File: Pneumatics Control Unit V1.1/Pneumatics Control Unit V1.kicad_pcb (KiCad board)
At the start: 2 copper layers, 35.8 x 27.4 mm, 38 parts, among them J1 TX_PORT, J2 10118194-0001LF, J3 RX_PORT, U1 SN65HVD1782D, U2 SN65HVD1782D, U3 FT2232D, Y1 Resonator_Small

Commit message: Linking foot prints
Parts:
- removed C10: 33n, Capacitor_SMD:C_0805_2012Metric_Pad1.18x1.45mm_HandSolder
- removed C9: 0.1u, Capacitor_SMD:C_0805_2012Metric_Pad1.18x1.45mm_HandSolder
- removed R10: 10k, Resistor_SMD:R_0805_2012Metric_Pad1.20x1.40mm_HandSolder
- removed R11: 1.5k, Resistor_SMD:R_0805_2012Metric_Pad1.20x1.40mm_HandSolder
- removed R8: 470, Resistor_SMD:R_0805_2012Metric_Pad1.20x1.40mm_HandSolder
- removed R9: 27, Resistor_SMD:R_0805_2012Metric_Pad1.20x1.40mm_HandSolder
- removed Y1: Resonator_Small, SamacSys_Parts:CSTCR_G
- added CR1: MBRS130L, MBRS130L:MBRS130L, F.Cu at (126.2, -194.4)
- added D10: D_TVS_x2_AAC, Package_TO_SOT_SMD:SOT-723, F.Cu at (141.1, -208.4)
- added D5: D_TVS_x2_AAC, Package_TO_SOT_SMD:SOT-723, F.Cu at (179.8, -213.7)
- added D6: D_TVS_x2_AAC, Package_TO_SOT_SMD:SOT-723, F.Cu at (167.0, -199.6)
- added D7: D_TVS_x2_AAC, Package_TO_SOT_SMD:SOT-723, F.Cu at (203.9, -235.5)
- added D8: D_TVS_x2_AAC, Package_TO_SOT_SMD:SOT-723, F.Cu at (186.7, -220.2)
- added D9: D_TVS_x2_AAC, Package_TO_SOT_SMD:SOT-723, F.Cu at (156.1, -188.8)
- added J10: Conn_01x02_Male, Connector_PinSocket_2.54mm:PinSocket_1x02_P2.54mm_Vertical, F.Cu at (182.9, -225.9)
- added J11: Conn_01x02_Male, Connector_PinSocket_2.54mm:PinSocket_1x02_P2.54mm_Vertical, F.Cu at (136.5, -191.4)
- added J4: Conn_01x02_Male, Connector_PinSocket_2.54mm:PinSocket_1x02_P2.54mm_Vertical, F.Cu at (141.1, -191.4)
- added J5: Conn_01x02_Male, Connector_PinSocket_2.54mm:PinSocket_1x02_P2.54mm_Vertical, F.Cu at (156.8, -201.6)
- added J6: Conn_01x02_Male, Connector_PinSocket_2.54mm:PinSocket_1x02_P2.54mm_Vertical, F.Cu at (152.2, -203.1)
- added J7: Conn_01x02_Male, Connector_PinSocket_2.54mm:PinSocket_1x02_P2.54mm_Vertical, F.Cu at (145.7, -191.4)
- added J8: Conn_01x02_Male, Connector_PinSocket_2.54mm:PinSocket_1x02_P2.54mm_Vertical, F.Cu at (136.5, -199.7)
- added J9: Conn_01x02_Male, Connector_PinSocket_2.54mm:PinSocket_1x02_P2.54mm_Vertical, F.Cu at (152.2, -196.0)
- added L1: SRR1205-500YL, induct:SRR1205500YL, F.Cu at (131.1, -209.9)
- added MOSFET1: SSM3K7002KFU, SSM3K7002KFU:SSM3K7002KFU, F.Cu at (176.3, -232.8)
- added MOSFET2: SSM3K7002KFU, SSM3K7002KFU:SSM3K7002KFU, F.Cu at (164.6, -220.2)
- added MOSFET3: SSM3K7002KFU, SSM3K7002KFU:SSM3K7002KFU, F.Cu at (144.1, -198.3)
- added MOSFET4: SSM3K7002KFU, SSM3K7002KFU:SSM3K7002KFU, F.Cu at (196.7, -232.8)
- added MOSFET5: SSM3K7002KFU, SSM3K7002KFU:SSM3K7002KFU, F.Cu at (174.8, -220.2)
- added MOSFET6: SSM3K7002KFU, SSM3K7002KFU:SSM3K7002KFU, F.Cu at (162.4, -208.5)
- added MOSFET7: SSM3K7002KFU, SSM3K7002KFU:SSM3K7002KFU, F.Cu at (172.6, -208.5)
- added MOSFET8: SSM3K7002KFU, SSM3K7002KFU:SSM3K7002KFU, F.Cu at (186.5, -232.8)
- C5: value 10n -> 100u; moved to F.Cu
- C6: value 10n -> 6.8n; moved to F.Cu
- C7: value 0.1u -> 0.01u; moved to F.Cu
- C8: value 0.1u -> 100u; moved to F.Cu
- D1: value RX_LED -> CDSOT23-SM712; footprint LED_SMD:LED_0805_2012Metric_Pad1.15x1.40mm_HandSolder -> CDSOT23-SM712:SOT-23-3
- D2: value TX_LED -> CDSOT23-SM712; footprint LED_SMD:LED_0805_2012Metric_Pad1.15x1.40mm_HandSolder -> CDSOT23-SM712:SOT-23-3
- D3, D4: value CDSOT23-SM712 -> D_TVS_x2_AAC; footprint CDSOT23-SM712:SOT-23-3 -> Package_TO_SOT_SMD:SOT-723
- J1: value TX_PORT -> RX_PORT; footprint Andrew_Custom:C189737 -> RS485:RS485
- J2: value 10118194-0001LF -> RX_PORT; footprint 10118194-0001LF:AMPHENOL_10118194-0001LF -> RS485:RS485
- J3: value RX_PORT -> MICROMOD-2222; footprint Andrew_Custom:C189737 -> m2:MDT420M02001
- R5, R6: value 330 -> 10000; moved to F.Cu
- R7: value 27 -> 10000; moved to F.Cu
- U1: value SN65HVD1782D -> ISL83490IBZ; footprint SN65HVD1782D:SOIC127P599X175-8N -> RS_UART:ISL83490IBZ
- U2: value SN65HVD1782D -> MIC2178-3.3YWM; footprint SN65HVD1782D:SOIC127P599X175-8N -> 33sw:MIC2178-3.3YWM
- U3: value FT2232D -> MC78M05CDTRKG; footprint Package_QFP:LQFP-48_7x7mm_P0.5mm -> 5v:MC78M05CDTRKG; moved to F.Cu
- moved R6 347.7 mm to (204.8, -238.4), turned to 0 degrees
- moved H2 344.1 mm to (188.4, -224.9)
- moved R7 338.6 mm to (194.1, -226.7), turned to 0 degrees
- moved U3 334.6 mm to (150.8, -230.8), turned to 0 degrees
- moved D4 334.4 mm to (182.6, -213.7), turned to 0 degrees
- moved J3 333.6 mm to (120.2, -227.2), turned to 0 degrees
- moved U1 331.8 mm to (166.3, -232.7), turned to 0 degrees
- moved R2 324.6 mm to (182.9, -216.6)
- moved R5 320.8 mm to (182.9, -219.6), turned to 0 degrees
- moved R3 316.0 mm to (168.0, -202.5)
- moved U2 310.9 mm to (115.3, -206.6), turned to 0 degrees
- moved J2 310.5 mm to (150.9, -210.3), turned to 0 degrees
- moved H3 307.0 mm to (157.7, -193.5)
- moved D2 305.5 mm to (141.5, -215.8), turned to 0 degrees
- moved C3 304.3 mm to (125.0, -200.5), turned to 0 degrees
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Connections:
- C1 pad 1: Net-(D3-Pad1) -> Net-(C1-Pad1)
- C2 pad 1: Net-(D3-Pad2) -> Net-(C2-Pad1)
- C3 pad 1: Net-(D4-Pad1) -> Net-(C3-Pad1)
- C4 pad 1: Net-(D4-Pad2) -> Net-(C4-Pad1)
- C5 pad 1: +5V -> GND
- C5 pad 2: GND -> /RS485_B_12V
- C6 pad 1: +5V -> Net-(C6-Pad1)
- C7 pad 1: +5V -> Net-(C7-Pad1)
- C8 pad 1: GND -> Net-(C8-Pad1)
- C8 pad 2: Net-(C9-Pad2) -> GND
- D1 pad 1: Net-(D1-Pad1) -> Net-(C1-Pad1)
- D1 pad 2: +5V -> Net-(C3-Pad1)
- D2 pad 1: Net-(D2-Pad1) -> Net-(C2-Pad1)
- D2 pad 2: +5V -> Net-(C4-Pad1)
- D3 pad 1: Net-(D3-Pad1) -> /GPIO_1
- D4 pad 1: Net-(D4-Pad1) -> /GPIO_0
- J1 pad 1: Net-(D3-Pad2) -> Net-(C3-Pad1)
- J1 pad 2: Net-(D3-Pad1) -> Net-(C1-Pad1)
- J1 pad 4: unconnected-(J1-Pad4) -> /RS485_B_12V
- J2 pad 1: +5V -> Net-(C4-Pad1)
- J2 pad 2: USB_D- -> Net-(C2-Pad1)
- J2 pad 3: USB_D+ -> GND
- J2 pad 4: GND -> /RS485_A_12V
- J3 pad 1: Net-(D4-Pad2) -> GND
- J3 pad 2: Net-(D4-Pad1) -> Net-(J3-Pad11)
- J3 pad 3: GND -> unconnected-(J3-Pad3)
- J3 pad 4: unconnected-(J2-Pad4) -> Net-(J3-Pad11)
- R1 pad 1: Net-(D3-Pad1) -> Net-(C3-Pad1)
- R1 pad 2: Net-(U2-Pad7) -> Net-(R1-Pad2)
- R2 pad 1: Net-(D3-Pad2) -> Net-(C1-Pad1)
- R2 pad 2: Net-(U2-Pad6) -> Net-(R2-Pad2)
- R3 pad 1: Net-(D4-Pad1) -> Net-(C4-Pad1)
- R3 pad 2: Net-(R4-Pad2) -> Net-(R3-Pad2)
- R4 pad 1: Net-(D4-Pad2) -> Net-(C2-Pad1)
- R4 pad 2: Net-(R3-Pad2) -> Net-(R4-Pad2)
- R5 pad 1: Net-(D2-Pad1) -> Net-(R5-Pad1)
- R5 pad 2: ~{USB_A_TXDLED} -> /RS485_B_12V
- R6 pad 1: Net-(D1-Pad1) -> Net-(R6-Pad1)
- R6 pad 2: ~{USB_A_RXDLED} -> Net-(C6-Pad1)
- R7 pad 1: USB_D- -> Net-(C7-Pad1)
- R7 pad 2: Net-(R7-Pad2) -> GND
- U1 pad 1: unconnected-(U2-Pad1) -> Net-(U1-Pad1)
- U1 pad 2: +5V -> /RS485_TXD
- U1 pad 3: +5V -> /RS485_RXD
- U1 pad 4: RS485_RXD -> Net-(U1-Pad4)
- U1 pad 5: GND -> Net-(R2-Pad2)
- U1 pad 6: Net-(U2-Pad6) -> Net-(R1-Pad2)
- U1 pad 7: Net-(U2-Pad7) -> Net-(R4-Pad2)
- U1 pad 8: +5V -> Net-(R3-Pad2)
- U2 pad 1: RS485_TXD -> /RS485_B_12V
- U2 pad 2: GND -> /RS485_B_12V
- U2 pad 3: GND -> Net-(U2-Pad3)
- U2 pad 4: unconnected-(U1-Pad4) -> GND
- U2 pad 6: Net-(R3-Pad2) -> GND
- U2 pad 7: Net-(R4-Pad2) -> GND
- U2 pad 8: +5V -> Net-(U2-Pad3)
- U3 pad 1: unconnected-(U3-Pad1) -> /RS485_A_12V
- U3 pad 3: +5V -> Net-(U3-Pad3)
- U3 pad 4: +5V -> GND
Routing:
- net GND: track 131.5 -> 0.00 mm, vias 15 -> 0
- net +5V: track 102.6 -> 0.00 mm, vias 3 -> 0
- net ~{USB_A_TXDLED}: track 46.5 -> 0.00 mm
- net ~{USB_A_RXDLED}: track 37.6 -> 0.00 mm
- net RS485_RXD: track 35.1 -> 0.00 mm, vias 1 -> 0
- net Net-(R7-Pad2): track 30.8 -> 0.00 mm
- net Net-(R8-Pad2): track 24.7 -> 0.00 mm
- net RS485_TXD: track 24.4 -> 0.00 mm, vias 1 -> 0
- net Net-(D4-Pad2): track 12.0 -> 0.00 mm
- net Net-(D3-Pad2): track 11.9 -> 0.00 mm
- net Net-(D4-Pad1): track 9.21 -> 0.00 mm
- net Net-(D3-Pad1): track 8.92 -> 0.00 mm
- net Net-(C9-Pad2): track 8.03 -> 0.00 mm
- net USB_D+: track 6.99 -> 0.00 mm, vias 1 -> 0
- net Net-(R10-Pad2): track 6.93 -> 0.00 mm
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- removed copper zone on B.Cu, net GND
- removed copper zone on F.Cu, net GND
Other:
- board outline removed

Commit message: Adding better m.2 connector
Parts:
- added C10: 0.1u, Capacitor_SMD:C_0805_2012Metric_Pad1.18x1.45mm_HandSolder, F.Cu at (127.2, 112.9)
- added C11: CL21A226MQQNNNF (22uF), 22U:CL21A226MQQNNNF, F.Cu at (195.9, 65.9)
- added C12: 22uF, 22U:CL21A226MQQNNNF, F.Cu at (171.2, 89.2)
- added C13: 22uF, 22U:CL21A226MQQNNNF, F.Cu at (171.2, 81.0)
- added C14: 22uF, 22U:CL21A226MQQNNNF, F.Cu at (178.5, 77.6)
- added C15: 22uF, 22U:CL21A226MQQNNNF, F.Cu at (195.6, 57.7)
- added C16: 22uF, 22U:CL21A226MQQNNNF, F.Cu at (150.4, 104.3)
- added C17: 22uF, 22U:CL21A226MQQNNNF, F.Cu at (188.6, 65.9)
- added C18: 22uF, 22U:CL21A226MQQNNNF, F.Cu at (157.7, 104.3)
- added C19: 22uF, 22U:CL21A226MQQNNNF, F.Cu at (150.4, 96.1)
- added C20: 22uF, 22U:CL21A226MQQNNNF, F.Cu at (157.7, 96.1)
- added C21: 22uF, 22U:CL21A226MQQNNNF, F.Cu at (188.3, 57.7)
- added C22: 1u, Capacitor_SMD:C_0805_2012Metric_Pad1.18x1.45mm_HandSolder, F.Cu at (129.6, 85.3)
- added C23: 1u, Capacitor_SMD:C_0805_2012Metric_Pad1.18x1.45mm_HandSolder, F.Cu at (150.0, 109.9)
- added C9: 0.1u, Capacitor_SMD:C_0805_2012Metric_Pad1.18x1.45mm_HandSolder, F.Cu at (141.6, 112.9)
- added H4: MountingHole, MountingHole:MountingHole_2.5mm, F.Cu at (190.8, 80.4)
- added H5: STAND-OFF-REFLOW2.5MM_TALL, MicroMod_ATP_CarrierBoard:STAND-OFF-REFLOW-M2.5, F.Cu at (110.4, 47.6)
- added J12: 10118194-0001LF, 10118194-0001LF:AMPHENOL_10118194-0001LF, F.Cu at (180.5, 70.1)
- C5, C8: value 100u -> 10n
- D1, D2: value CDSOT23-SM712 -> D_TVS_x2_AAC; footprint CDSOT23-SM712:SOT-23-3 -> Package_TO_SOT_SMD:SOT-723
- J3: footprint m2:MDT420M02001 -> mm-m:M.2-CONNECTOR-E
- L1: value SRR1205-500YL -> LB3218T330M (33uH); footprint induct:SRR1205500YL -> induct33u:LB3218T330M
- R5: value 10000 -> 20k
- R6, R7: value 10000 -> 10k
- U3: footprint 5v:MC78M05CDTRKG -> 12v5v:MC78M05CDTRKG
- moved MOSFET8 344.0 mm to (131.7, 106.8)
- moved MOSFET1 341.4 mm to (141.9, 106.8)
- moved R6 329.2 mm to (178.0, 89.7)
- moved R7 329.0 mm to (169.2, 101.4)
- moved D4 323.1 mm to (163.6, 108.8)
- moved H2 322.1 mm to (170.1, 96.6)
- moved D10 321.8 mm to (159.9, 112.8)
- moved MOSFET5 318.3 mm to (131.7, 95.2)
- moved C3 314.9 mm to (156.0, 112.9)
- moved C2 313.9 mm to (146.4, 112.9)
- moved U1 307.7 mm to (157.3, 75.0)
- moved D7 306.9 mm to (201.2, 71.4)
- moved R5 305.3 mm to (184.6, 85.7)
- moved MOSFET6 304.4 mm to (141.9, 95.2)
- moved CR1 301.7 mm to (116.8, 107.2)
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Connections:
- C5 pad 1: GND -> Net-(C10-Pad1)
- C5 pad 2: /RS485_B_12V -> GND
- C8 pad 1: Net-(C8-Pad1) -> Net-(C10-Pad1)
- CR1 pad 1: Net-(U2-Pad3) -> Net-(CR1-Pad1)
- J3 pad 3: unconnected-(J3-Pad3) -> /USB_D+
- J3 pad 5: unconnected-(J3-Pad5) -> /USB_D-
- J3 pad 9: unconnected-(J3-Pad9) -> Net-(J3-Pad9)
- L1 pad 1: Net-(U2-Pad3) -> /220uF
- L1 pad 2: Net-(C8-Pad1) -> Net-(CR1-Pad1)
- R5 pad 2: /RS485_B_12V -> /RS485_A_12V
- U2 pad 1: /RS485_B_12V -> /RS485_A_12V
- U2 pad 12: Net-(C8-Pad1) -> /220uF
- U2 pad 2: /RS485_B_12V -> /RS485_A_12V
- U2 pad 20: /RS485_B_12V -> /RS485_A_12V
- U2 pad 3: Net-(U2-Pad3) -> Net-(CR1-Pad1)
- U2 pad 8: Net-(U2-Pad3) -> Net-(CR1-Pad1)
- U2 pad 9: /RS485_B_12V -> /RS485_A_12V
- U3 pad 1: /RS485_A_12V -> /RS485_B_12V

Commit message: PCB Fun times :)
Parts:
- C1, C2, C3, C4, D1, D2, H5, J3, R1, R2, R3, R4, U1: moved to B.Cu
- moved R5 142.0 mm to (44.1, 106.0)
- moved C15 137.4 mm to (62.0, 89.7)
- moved C11 137.0 mm to (61.5, 92.5)
- moved C21 134.8 mm to (57.4, 89.9)
- moved C17 133.8 mm to (57.5, 92.5)
- moved C12 127.1 mm to (44.1, 92.2)
- moved C14 110.6 mm to (68.5, 89.3)
- moved C18 109.7 mm to (48.6, 92.5)
- moved C20 109.3 mm to (48.6, 89.5)
- moved R2 108.5 mm to (128.3, 118.5), turned to 180 degrees
- moved C13 104.1 mm to (67.8, 92.5)
- moved R1 99.1 mm to (129.7, 121.2), turned to 180 degrees
- moved C16 98.5 mm to (52.7, 92.3)
- moved C19 97.5 mm to (53.1, 89.9)
- moved J5 96.2 mm to (112.8, 75.5)
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
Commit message: Consolidated PCB
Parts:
- C10, C5, C8, C9, D10, D3, D4, D5, D6, D7, D8, D9, MOSFET1, MOSFET2, MOSFET3, MOSFET4, MOSFET5, MOSFET6, MOSFET7, MOSFET8: moved to B.Cu
- moved R5 77.9 mm to (119.9, 88.4), turned to 90 degrees
- moved C12 77.8 mm to (121.5, 100.1), turned to 90 degrees
- moved C16 74.3 mm to (126.6, 100.2), turned to 90 degrees
- moved C18 72.9 mm to (121.5, 95.5), turned to 90 degrees
- moved U2 71.2 mm to (130.2, 86.9)
- moved C20 70.0 mm to (118.4, 95.5), turned to 90 degrees
- moved C15 67.4 mm to (129.1, 95.7), turned to 90 degrees
- moved C21 67.4 mm to (124.0, 100.2), turned to 90 degrees
- moved C17 66.6 mm to (124.0, 95.7), turned to 90 degrees
- moved C19 66.1 mm to (118.4, 100.1), turned to 90 degrees
- moved CR1 65.1 mm to (130.7, 77.9)
- moved C6 62.7 mm to (137.7, 99.6), turned to 90 degrees
- moved C14 61.6 mm to (129.1, 100.1), turned to 90 degrees
- moved L1 59.7 mm to (122.9, 79.2)
- moved C13 58.9 mm to (126.6, 95.5), turned to 90 degrees
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
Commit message: Technically its wired
This is a little messy, but it is wired
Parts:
- moved MOSFET8 1.66 mm to (150.9, 91.0)
- moved D10 1.50 mm to (150.6, 88.0)
- moved MOSFET3 1.30 mm to (110.0, 102.6)
- moved D7 1.28 mm to (110.2, 109.0)
- moved U1 1.14 mm to (121.9, 114.8), turned to 0 degrees
- moved D5 1.14 mm to (110.0, 99.8)
- moved J11 1.09 mm to (154.2, 88.2)
- moved J7 1.08 mm to (154.3, 98.7)
- moved D6 1.08 mm to (150.9, 98.0)
- moved MOSFET4 1.08 mm to (151.2, 100.9)
- moved MOSFET5 1.02 mm to (110.2, 111.8)
- moved D9 0.95 mm to (150.5, 109.4)
- moved J10 0.95 mm to (153.9, 110.5)
- moved MOSFET7 0.95 mm to (150.6, 112.9)
- moved MOSFET1 0.88 mm to (110.0, 89.9)
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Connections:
- C23 pad 1: Net-(C23-Pad1) -> 5V
- J10 pad 2: Net-(J10-Pad2) -> 5V
- J11 pad 2: Net-(J11-Pad2) -> 5V
- J12 pad 1: Net-(J12-Pad1) -> USB_V
- J3 pad 9: Net-(J3-Pad9) -> USB_V
- J4 pad 2: Net-(J4-Pad2) -> 5V
- J5 pad 2: Net-(J5-Pad2) -> 5V
- J6 pad 2: Net-(J6-Pad2) -> 5V
- J7 pad 2: Net-(J7-Pad2) -> 5V
- J8 pad 2: Net-(J8-Pad2) -> 5V
- J9 pad 2: Net-(J9-Pad2) -> 5V
- U1 pad 1: Net-(U1-Pad1) -> 5V
- U3 pad 3: Net-(C23-Pad1) -> 5V
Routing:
- net GND: track 0.00 -> 393.8 mm, vias 0 -> 23
- net 5V: track 0.00 -> 195.8 mm, vias 0 -> 3
- net /RS485_A_12V: track 0.00 -> 84.7 mm, vias 0 -> 2
- net /USB_D-: track 0.00 -> 50.2 mm, vias 0 -> 5
- net /220uF: track 0.00 -> 47.6 mm, vias 0 -> 4
- net USB_V: track 0.00 -> 45.4 mm, vias 0 -> 3
- net /GPIO_4: track 0.00 -> 42.7 mm
- net /USB_D+: track 0.00 -> 42.2 mm, vias 0 -> 3
- net Net-(R6-Pad1): track 0.00 -> 41.8 mm, vias 0 -> 6
- net Net-(J3-Pad11): track 0.00 -> 41.4 mm, vias 0 -> 3
- net /GPIO_3: track 0.00 -> 38.0 mm
- net /GPIO_7: track 0.00 -> 36.0 mm, vias 0 -> 2
- net /GPIO_1: track 0.00 -> 32.7 mm, vias 0 -> 2
- net /GPIO_6: track 0.00 -> 32.3 mm, vias 0 -> 2
- net /GPIO_2: track 0.00 -> 31.7 mm
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
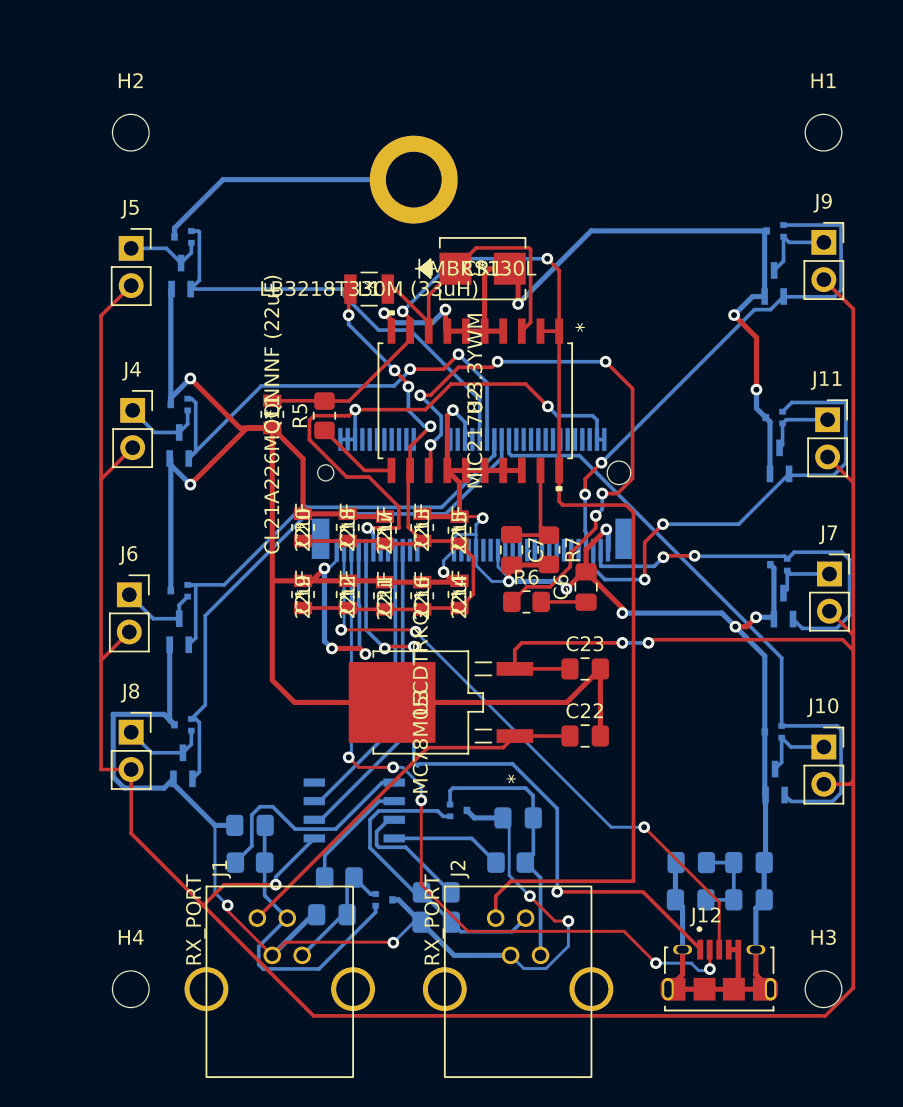
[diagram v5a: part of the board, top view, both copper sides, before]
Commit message: Cleaning up grounds
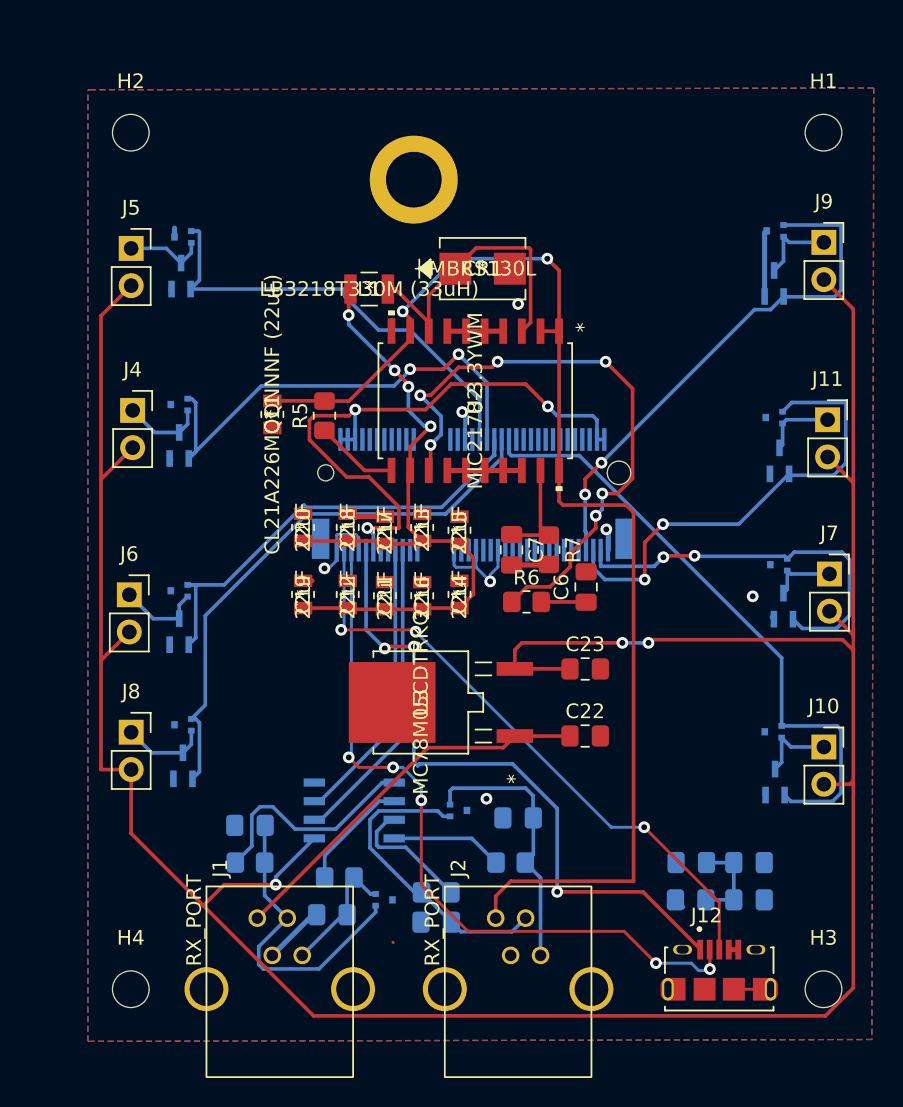
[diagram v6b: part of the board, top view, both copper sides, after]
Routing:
- net GND: track 393.8 -> 50.3 mm, vias 23 -> 7
- added copper zone on B.Cu, net GND
- added copper zone on F.Cu, net GND

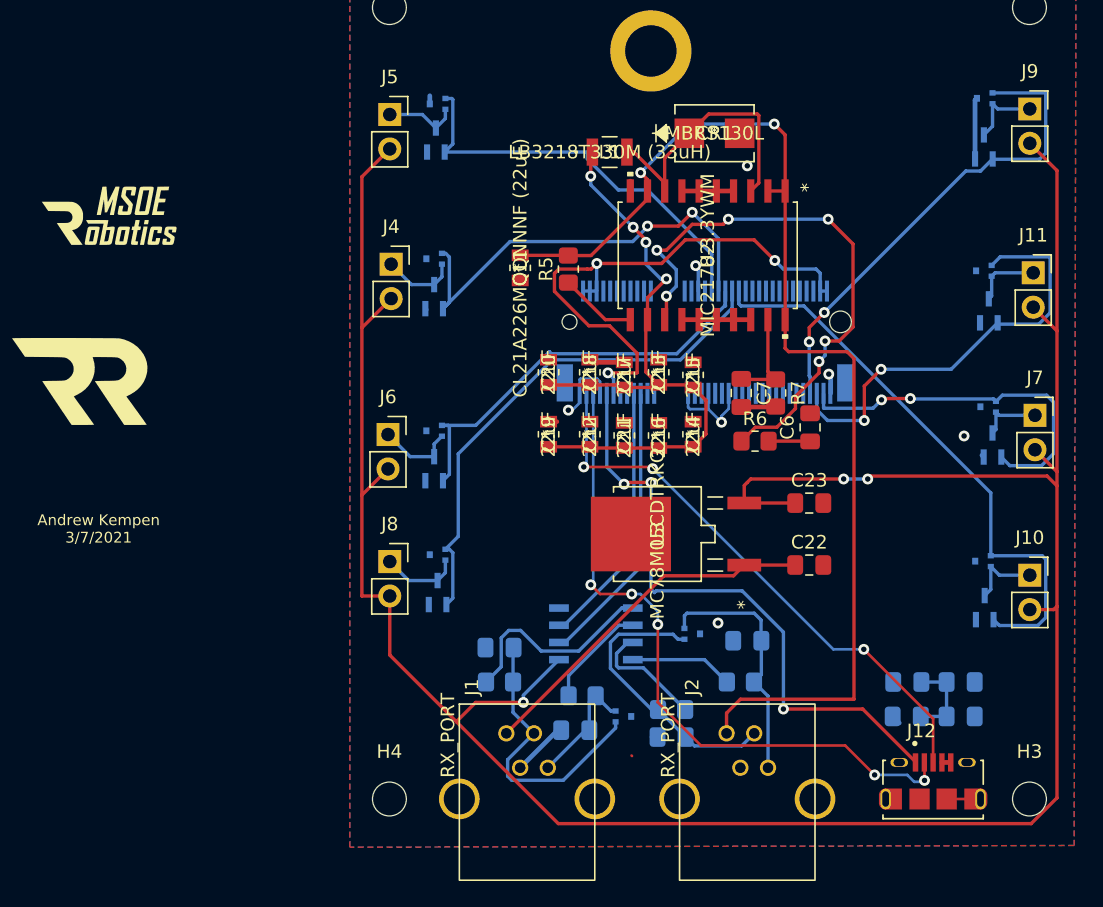
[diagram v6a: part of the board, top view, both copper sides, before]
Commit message: Fixing errors and adding another 5V
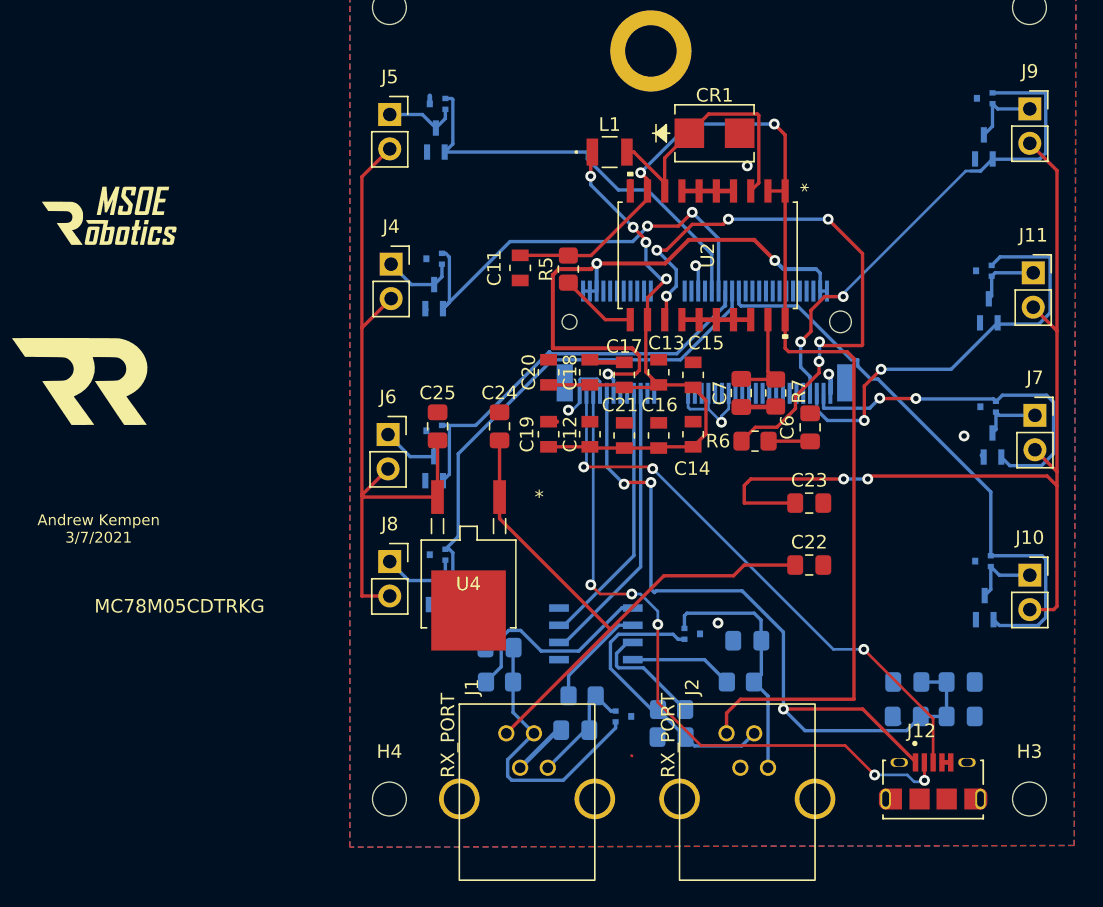
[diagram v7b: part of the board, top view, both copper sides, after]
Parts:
- removed U3: MC78M05CDTRKG, 12v5v:MC78M05CDTRKG
- added C24: 1u, Capacitor_SMD:C_0805_2012Metric_Pad1.18x1.45mm_HandSolder, F.Cu at (114.8, 99.5)
- added C25: 1u, Capacitor_SMD:C_0805_2012Metric_Pad1.18x1.45mm_HandSolder, F.Cu at (110.2, 99.5)
- added U4: MC78M05CDTRKG, 12v5v:MC78M05CDTRKG, F.Cu at (112.5, 111.1)
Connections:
- C10 pad 1: Net-(C10-Pad1) -> USB_V
- C5 pad 1: Net-(C10-Pad1) -> USB_V
- C8 pad 1: Net-(C10-Pad1) -> USB_V
- C9 pad 1: Net-(C10-Pad1) -> USB_V
- U1 pad 1: 5V -> Net-(U1-Pad1)
- U1 pad GND: Net-(U1-Pad4) -> (no net)
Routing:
- net 5V: track 195.8 -> 122.1 mm, vias 3 -> 2
- net USB_V: track 45.4 -> 63.0 mm
- net /RS485_B_12V: track 26.5 -> 43.8 mm
- net GND: track 50.3 -> 43.3 mm
- net Net-(C10-Pad1): track 6.31 -> 0.00 mm
- net Net-(J3-Pad11): track 41.4 -> 44.1 mm
- net Net-(R6-Pad1): track 41.8 -> 43.9 mm
- net /GPIO_7: track 36.0 -> 37.4 mm
